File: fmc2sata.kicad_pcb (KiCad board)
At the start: 4 copper layers, 108 x 69 mm, 63 parts, among them J1 ASP-134488-01, J2 1-2199230-6, J3 te-770829-1, Q1 BSS138APW, Q2 BSS138APW, Q3 DMG2305UX-13, Q4 BSS138APW, U1 TPS565208, U2 TPS565208, Y1 AX3DAF1-150.0000

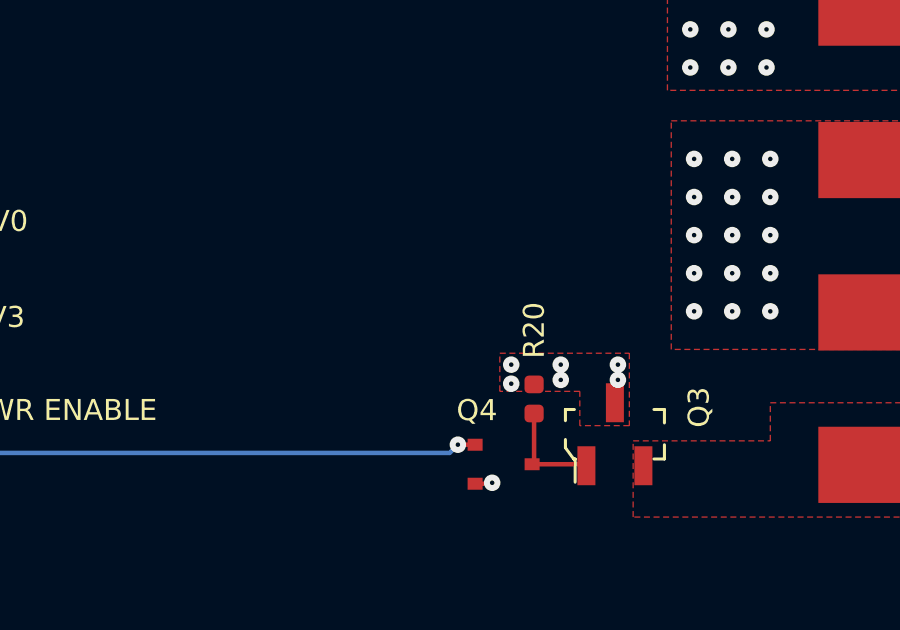
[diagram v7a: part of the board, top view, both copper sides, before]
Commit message: Add testpads for power supply - DRC clean
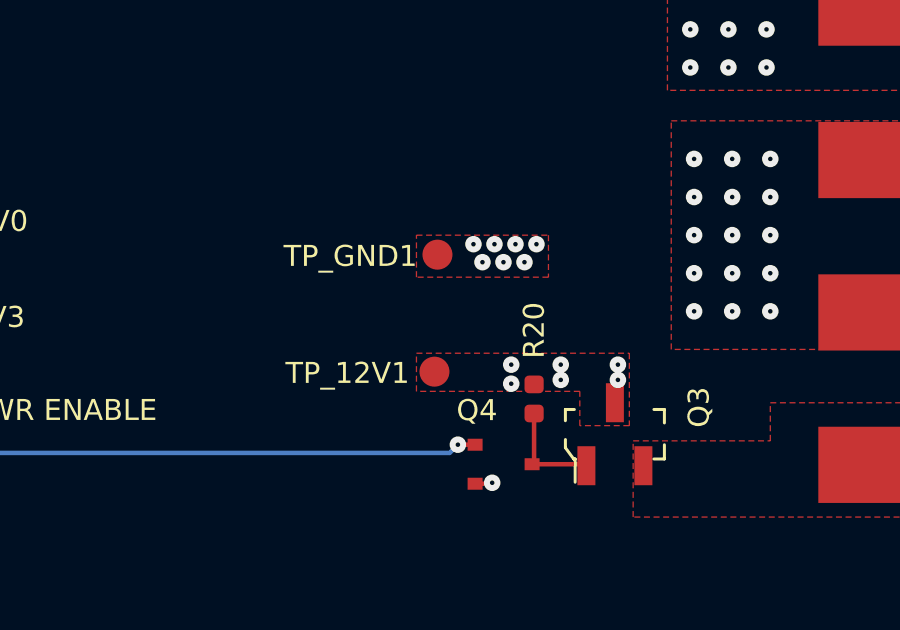
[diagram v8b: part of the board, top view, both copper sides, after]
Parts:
- added TP_12V1: TP_SMD1MM, antmicro-footprints:Testpoint_smd_1mm, F.Cu at (125.3, 65.6)
- added TP_GND1: TP_SMD1MM, antmicro-footprints:Testpoint_smd_1mm, F.Cu at (125.4, 61.7)
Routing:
- net GND: vias 156 -> 163
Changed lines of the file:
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@@
     (thickness 1.6)
     (drawings 13)
-    (tracks 1020)
+    (tracks 1027)
     (zones 0)
-    (modules 63)
+    (modules 65)
     (nets 166)
   )
@@
     (add_net SATA_CLK_P)
   )
+  (module antmicro-footprints:Testpoint_smd_1mm (layer F.Cu)
+    (at 125.385 61.665)
+    (attr virtual)
+    (fp_text reference TP_GND1 (at -2.9 0) (layer F.SilkS)
+      (effects (font (size 0.7 0.7) (thickness 0.15)))
+    )
+    (fp_text value TP_SMD1MM (at 0 -0.5) (layer F.Fab) hide
+      (effects (font (size 1 1) (thickness 0.15)))
+    )
+    (pad 1 smd circle (at 0 -0.0508) (size 1 1) (layers F.Cu F.Mask)
+      (net 2 GND))
+  )
+  (module antmicro-footprints:Testpoint_smd_1mm (layer F.Cu)
+    (at 125.285 65.565)
+    (attr virtual)
+    (fp_text reference TP_12V1 (at -2.9 0) (layer F.SilkS)
+      (effects (font (size 0.7 0.7) (thickness 0.15)))
+    )
+    (fp_text value TP_SMD1MM (at 0 -0.5) (layer F.Fab) hide
+      (effects (font (size 1 1) (thickness 0.15)))
+    )
+    (pad 1 smd circle (at 0 -0.0508) (size 1 1) (layers F.Cu F.Mask)
+      (net 1 +12V))
+  )
   (module fmc2sata-footprints:ASP-134488-01 (layer B.Cu)
     (at 80.6 77.6 270)
@@
   (via (at 132.602 46.1) (size 5.4) (drill 2.7) (layers F.Cu B.Cu) (net 0))
   (via (at 132.6 109.1) (size 5.4) (drill 2.7) (layers F.Cu B.Cu) (net 0))
+  (via (at 126.585 61.265) (size 0.55) (drill 0.15) (layers F.Cu B.Cu) (net 2))
   (segment (start 77.425 54.105) (end 76.79 53.47) (width 0.15) (layer B.Cu) (net 165))
   (via (at 76.79 53.47) (size 0.55) (drill 0.15) (layers F.Cu B.Cu) (net 165))
@@
   (segment (start 83.775 99.825) (end 84.385 99.215) (width 0.15) (layer B.Cu) (net 2))
   (segment (start 84.385 99.215) (end 84.385 97.965) (width 0.15) (layer B.Cu) (net 2))
+  (via (at 127.285 61.265) (size 0.55) (drill 0.15) (layers F.Cu B.Cu) (net 2))
+  (via (at 127.985 61.265) (size 0.55) (drill 0.15) (layers F.Cu B.Cu) (net 2))
+  (via (at 128.685 61.265) (size 0.55) (drill 0.15) (layers F.Cu B.Cu) (net 2))
+  (via (at 128.285 61.865) (size 0.55) (drill 0.15) (layers F.Cu B.Cu) (net 2))
+  (via (at 127.585 61.865) (size 0.55) (drill 0.15) (layers F.Cu B.Cu) (net 2))
+  (via (at 126.885 61.865) (size 0.55) (drill 0.15) (layers F.Cu B.Cu) (net 2))
   (segment (start 94.85 76.03) (end 93.85 76.03) (width 0.5) (layer F.Cu) (net 3))
   (segment (start 95.16 75.72) (end 94.85 76.03) (width 0.5) (layer F.Cu) (net 3))
@@
     (polygon
       (pts
-        (xy 131.781 67.313) (xy 130.13 67.313) (xy 130.13 66.17) (xy 127.463 66.17) (xy 127.463 64.9)
+        (xy 131.781 67.313) (xy 130.13 67.313) (xy 130.13 66.17) (xy 124.685 66.17) (xy 124.685 64.9)
         (xy 131.781 64.9)
       )
@@
       )
     )
+  )
+  (zone (net 2) (net_name GND) (layer F.Cu) (hatch edge 0.508)
+    (connect_pads yes (clearance 0.25))
+    (min_thickness 0.254)
+    (fill yes (arc_segments 32) (thermal_gap 0.508) (thermal_bridge_width 0.508))
+    (polygon
+      (pts
+        (xy 129.085 62.365) (xy 124.685 62.365) (xy 124.685 60.965) (xy 129.085 60.965)
+      )
+    )
